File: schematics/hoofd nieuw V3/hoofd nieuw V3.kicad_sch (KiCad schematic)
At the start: 42 parts, among them J1 Conn_01x04_Pin, J2 Conn_01x02_Pin, J3 SFR02, J4 Conn_01x03_Pin, J5 Conn_01x01, J6 Conn_01x01, J7 Conn_01x01, J8 Conn_01x01, U1 ATtiny402-SS, Y1 ECS-2333MV-100-BN-TR

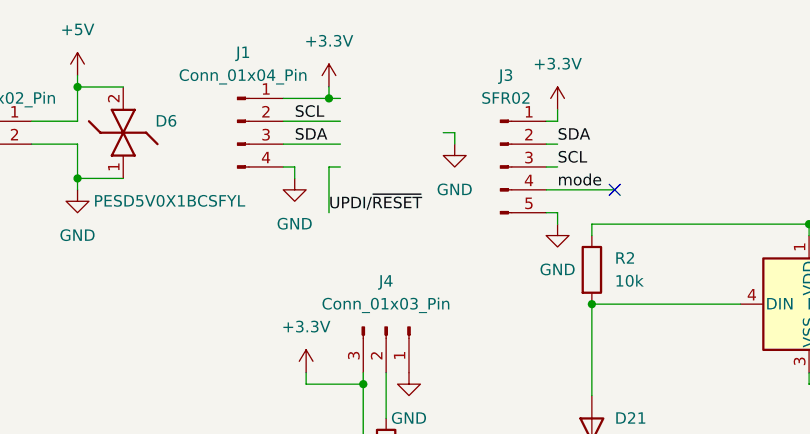
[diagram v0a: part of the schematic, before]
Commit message: voeg nog ESD bescherming toe aan nieuw hoofd V3
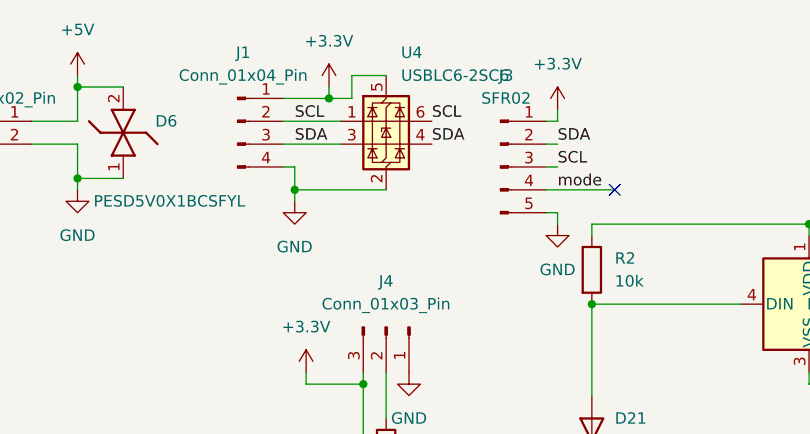
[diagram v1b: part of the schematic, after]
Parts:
- added U4: USBLC6-2SC6, Package_TO_SOT_SMD:SOT-23-6, symbol Power_Protection:USBLC6-2SC6
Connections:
- net +3.3V: now also U4.5 (VBUS)
- net GND: now also U4.2 (GND)
- net SCL: now also U4.1 (I/O1), U4.6 (I/O1)
- net SDA: now also U4.3 (I/O2), U4.4 (I/O2)
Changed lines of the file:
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@@
 	)
 	(junction
+		(at 49.53 33.02)
+		(diameter 0)
+		(color 0 0 0 1)
+	)
+	(junction
 		(at 106.68 67.31)
 		(diameter 0)
@@
 	(wire
 		(pts
-			(xy 54.61 30.48) (xy 53.34 30.48)
-		)
-		(stroke
-			(width 0)
-			(type default)
-		)
-	)
-	(wire
-		(pts
 			(xy 106.68 97.79) (xy 128.27 97.79)
 		)
@@
 	(wire
 		(pts
-			(xy 48.26 30.48) (xy 49.53 30.48)
+			(xy 49.53 30.48) (xy 48.26 30.48)
 		)
 		(stroke
@@
 	(wire
 		(pts
-			(xy 54.61 22.86) (xy 53.34 22.86)
+			(xy 53.34 22.86) (xy 55.88 22.86)
 		)
 		(stroke
@@
 	(wire
 		(pts
-			(xy 53.34 30.48) (xy 53.34 35.56)
+			(xy 123.19 168.91) (xy 125.73 168.91)
 		)
 		(stroke
@@
 	(wire
 		(pts
-			(xy 123.19 168.91) (xy 125.73 168.91)
+			(xy 49.53 33.02) (xy 59.69 33.02)
 		)
 		(stroke
 			(width 0)
 			(type default)
+			(color 0 0 0 1)
 		)
 	)
@@
 	(wire
 		(pts
-			(xy 49.53 30.48) (xy 49.53 31.75)
+			(xy 49.53 30.48) (xy 49.53 33.02)
 		)
 		(stroke
@@
 	(wire
 		(pts
+			(xy 55.88 20.32) (xy 59.69 20.32)
+		)
+		(stroke
+			(width 0)
+			(type default)
+			(color 255 0 0 1)
+		)
+	)
+	(wire
+		(pts
 			(xy 236.22 83.82) (xy 236.22 85.09)
 		)
@@
 	(wire
 		(pts
-			(xy 66.04 26.67) (xy 67.31 26.67)
-		)
-		(stroke
-			(width 0)
-			(type default)
-			(color 0 0 0 1)
-		)
-	)
-	(wire
-		(pts
 			(xy 257.81 66.04) (xy 257.81 67.31)
 		)
@@
 	(wire
 		(pts
+			(xy 49.53 34.29) (xy 49.53 33.02)
+		)
+		(stroke
+			(width 0)
+			(type default)
+			(color 0 0 0 1)
+		)
+	)
+	(wire
+		(pts
 			(xy 123.19 147.32) (xy 125.73 147.32)
 		)
@@
 	(wire
 		(pts
-			(xy 67.31 26.67) (xy 67.31 27.94)
-		)
-		(stroke
-			(width 0)
-			(type default)
-			(color 0 0 0 1)
-		)
-	)
-	(wire
-		(pts
 			(xy 144.78 156.21) (xy 144.78 134.62)
 		)
@@
 	(wire
 		(pts
+			(xy 55.88 22.86) (xy 55.88 20.32)
+		)
+		(stroke
+			(width 0)
+			(type default)
+			(color 255 0 0 1)
+		)
+	)
+	(wire
+		(pts
 			(xy 149.86 67.31) (xy 149.86 68.58)
 		)
@@
 		)
 	)
+	(label "SDA"
+		(at 64.77 27.94 0)
+		(effects
+			(font
+				(size 1.27 1.27)
+			)
+			(justify left bottom)
+		)
+	)
 	(label "SCL"
 		(at 78.74 30.48 0)
@@
 		)
 	)
-	(label "UPDI{slash}~{RESET}"
-		(at 53.34 35.56 0)
+	(label "SCL"
+		(at 64.77 25.4 0)
 		(effects
 			(font
@@
 	)
 	(symbol
-		(lib_id "power:GND")
-		(at 67.31 27.94 0)
-		(unit 1)
-		(exclude_from_sim no)
-		(in_bom yes)
-		(on_board yes)
-		(dnp no)
-		(fields_autoplaced yes)
-		(property "Reference" "#PWR020"
-			(at 67.31 34.29 0)
-			(effects
-				(font
-					(size 1.27 1.27)
-				)
-				(hide yes)
-			)
-		)
-		(property "Value" "GND"
-			(at 67.31 33.02 0)
-			(effects
-				(font
-					(size 1.27 1.27)
-				)
-			)
-		)
-		(property "Footprint" ""
-			(at 67.31 27.94 0)
-			(effects
-				(font
-					(size 1.27 1.27)
-				)
-				(hide yes)
-			)
-		)
-		(property "Datasheet" ""
-			(at 67.31 27.94 0)
-			(effects
-				(font
-					(size 1.27 1.27)
-				)
-				(hide yes)
-			)
-		)
-		(property "Description" "Power symbol creates a global label with name \"GND\" , ground"
-			(at 67.31 27.94 0)
-			(effects
-				(font
-					(size 1.27 1.27)
-				)
-				(hide yes)
-			)
-		)
-		(pin "1"
-		)
-		(instances
-			(project "hoofd nieuw"
-				(path "/7e0a6d27-e85c-4a07-8035-4491285a0fea"
-					(reference "#PWR020")
-					(unit 1)
-				)
-			)
-		)
-	)
-	(symbol
 		(lib_id "Device:C")
 		(at 90.17 76.2 0)
@@
 	(symbol
 		(lib_id "power:GND")
-		(at 49.53 31.75 0)
+		(at 49.53 34.29 0)
 		(unit 1)
 		(exclude_from_sim no)
@@
 		(fields_autoplaced yes)
 		(property "Reference" "#PWR01"
-			(at 49.53 38.1 0)
+			(at 49.53 40.64 0)
 			(effects
 				(font
@@
 		)
 		(property "Value" "GND"
-			(at 49.53 36.83 0)
+			(at 49.53 39.37 0)
 			(effects
 				(font
@@
 		)
 		(property "Footprint" ""
-			(at 49.53 31.75 0)
+			(at 49.53 34.29 0)
 			(effects
 				(font
@@
 		)
 		(property "Datasheet" ""
-			(at 49.53 31.75 0)
+			(at 49.53 34.29 0)
 			(effects
 				(font
@@
 		)
 		(property "Description" "Power symbol creates a global label with name \"GND\" , ground"
-			(at 49.53 31.75 0)
+			(at 49.53 34.29 0)
 			(effects
 				(font
@@
 					(unit 1)
 				)
+			)
+		)
+	)
+	(symbol
+		(lib_id "Power_Protection:USBLC6-2SC6")
+		(at 59.69 25.4 0)
+		(unit 1)
+		(exclude_from_sim no)
+		(in_bom yes)
+		(on_board yes)
+		(dnp no)
+		(fields_autoplaced yes)
+		(property "Reference" "U4"
+			(at 61.3411 17.78 0)
+			(effects
+				(font
+					(size 1.27 1.27)
+				)
+				(justify left)
+			)
+		)
+		(property "Value" "USBLC6-2SC6"
+			(at 61.3411 20.32 0)
+			(effects
+				(font
+					(size 1.27 1.27)
+				)
+				(justify left)
+			)
+		)
+		(property "Footprint" "Package_TO_SOT_SMD:SOT-23-6"
+			(at 60.96 31.75 0)
+			(effects
+				(font
+					(size 1.27 1.27)
+					(italic yes)
+				)
+				(justify left)
+				(hide yes)
+			)
+		)
+		(property "Datasheet" "https://www.st.com/resource/en/datasheet/usblc6-2.pdf"
+			(at 60.96 33.655 0)
+			(effects
+				(font
+					(size 1.27 1.27)
+				)
+				(justify left)
+				(hide yes)
+			)
+		)
+		(property "Description" "Very low capacitance ESD protection diode, 2 data-line, SOT-23-6"
+			(at 59.69 25.4 0)
+			(effects
+				(font
+					(size 1.27 1.27)
+				)
+				(hide yes)
+			)
+		)
+		(pin "1"
+		)
+		(pin "3"
+		)
+		(pin "4"
+		)
+		(pin "5"
+		)
+		(pin "6"
+		)
+		(pin "2"
+		)
+		(instances
+			(project ""
+				(path "/7e0a6d27-e85c-4a07-8035-4491285a0fea"
+					(reference "U4")
+					(unit 1)
+				)
